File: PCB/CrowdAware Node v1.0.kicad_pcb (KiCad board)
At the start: 2 copper layers, 61 x 36.5 mm, 10 parts, among them J1 Heltec WiFi LoRa 32(V3)

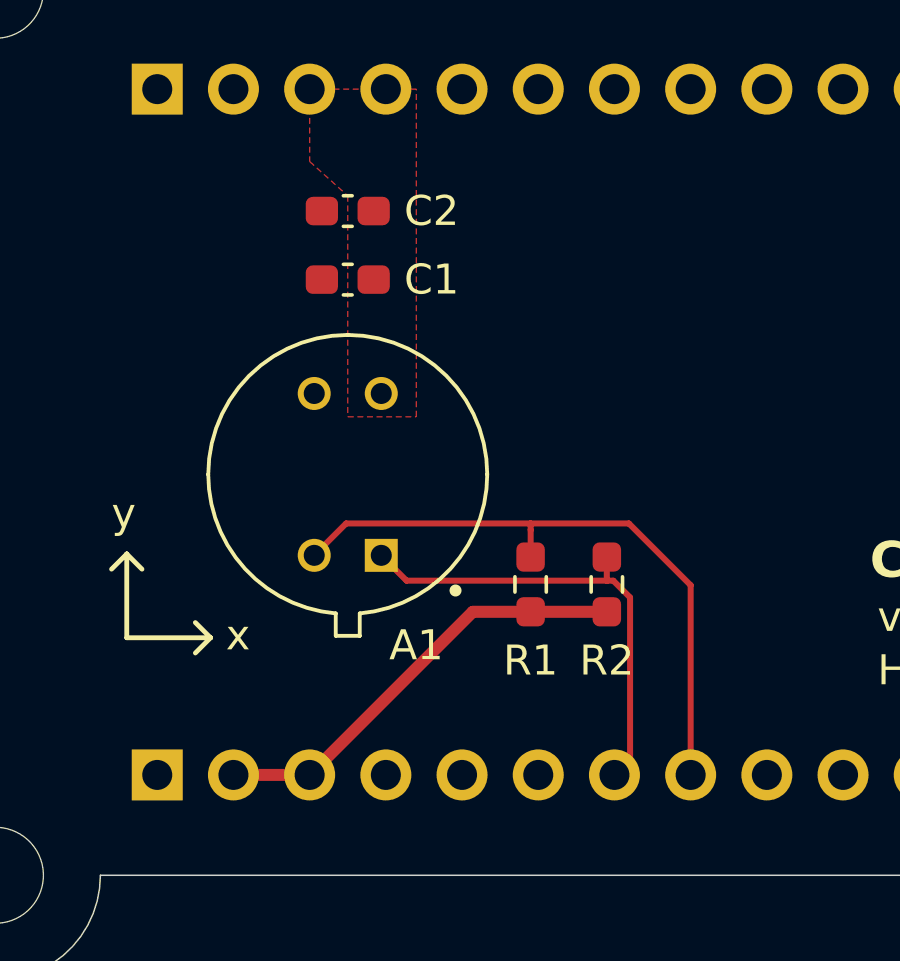
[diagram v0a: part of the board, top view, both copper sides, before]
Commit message: Include BOM, Adjusted footprints to match
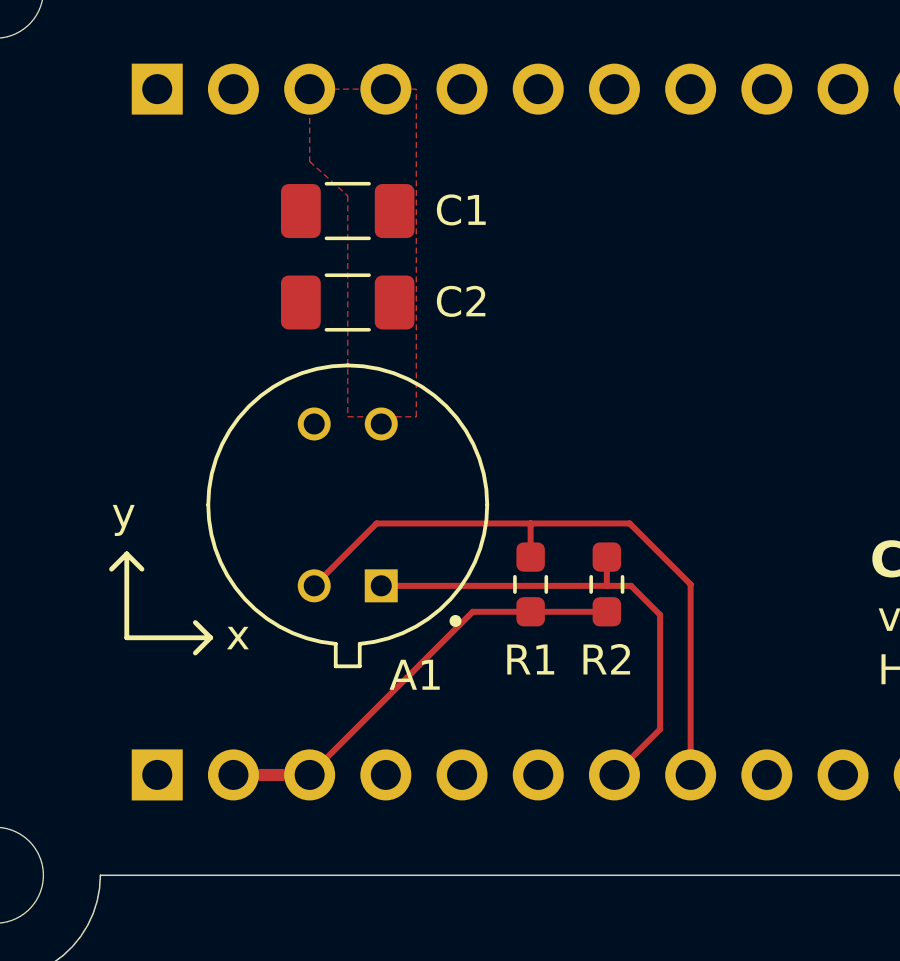
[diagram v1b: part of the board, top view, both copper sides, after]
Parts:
- C1: renamed from C2; value 100u -> 100u 10V 1206; footprint MyLib:C_0603_1608Metric_Pad1.08x0.95mm_HandSolder -> Capacitor_SMD:C_1206_3216Metric_Pad1.33x1.80mm_HandSolder
- C2: renamed from C1; value 10u 0603 -> 10u 10V 1206; footprint MyLib:C_0603_1608Metric_Pad1.08x0.95mm_HandSolder -> Capacitor_SMD:C_1206_3216Metric_Pad1.33x1.80mm_HandSolder
- J1: value Heltec WiFi LoRa 32(V3) -> 2 pcs 1x20 socket 2.54mm
- R1: value 1k 0603 -> 1k 0603 10%
- R2: value 1k -> 1k 0603 10%
- moved A1 1.02 mm to (88.9, 75.3)
- moved C2 0.76 mm to (88.9, 68.6)
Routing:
- net /SDA: track 15.8 -> 16.6 mm
